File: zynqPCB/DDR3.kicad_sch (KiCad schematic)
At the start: 62 parts, among them U15 MT41K256M16HA-125_E, U16 MT41K256M16HA-125_E, U20H xc7z020clg484, U8 TPS51200DRCR

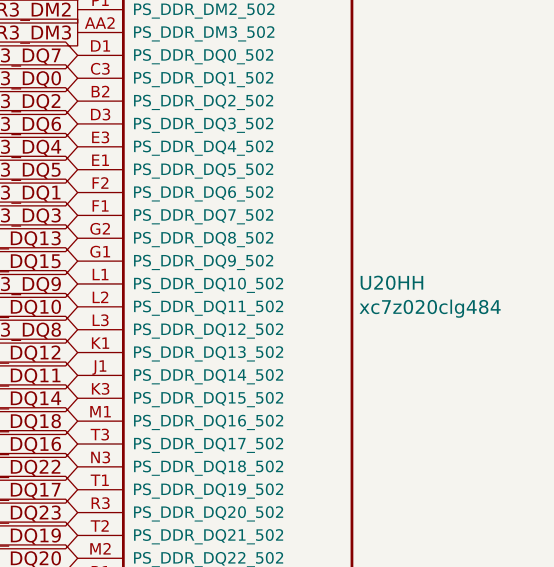
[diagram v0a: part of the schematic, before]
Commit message: Update audio schematic
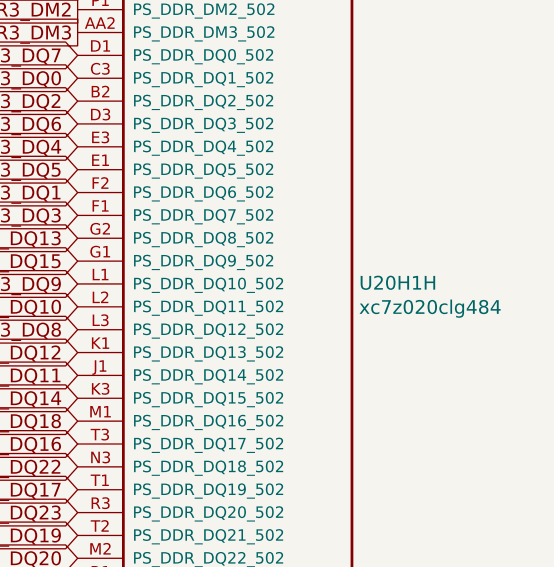
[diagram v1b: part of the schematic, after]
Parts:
- renumbered U20H to U20H1
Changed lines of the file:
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@@
 		(on_board yes)
 		(dnp no)
-		(property "Reference" "U20H"
+		(property "Reference" "U20H1"
 			(at 289.0774 105.3338 0)
 			(effects
@@
 			(project "DFTBoard"
 				(path "/49eba173-d38c-4d05-b21c-b4a14c4948c2/00000000-0000-0000-0000-000058818a06"
-					(reference "U20H")
+					(reference "U20H1")
 					(unit 8)
 				)
